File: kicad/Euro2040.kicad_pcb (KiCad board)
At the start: 2 copper layers, 15 x 58.4 mm, 70 parts, among them J1 USB_B_Micro, J3 Conn_02x05_Odd_Even, J5 Conn_01x10_Male, SW1 SW_MEC_5E, U1 RP2040, U2 RT6150B-33GQW, U3 W25Q16JVUXIQ, U4 L7805, U5 TL074, U6 TL074, U7 LM4040DBZ-3, X1 Crystal_GND24

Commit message: save
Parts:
- moved C20 98.9 mm to (-71.2, 21.5)
- moved C22 98.9 mm to (-72.7, 32.4)
- moved R16 98.9 mm to (-52.5, 29.8)
- moved R17 98.9 mm to (-35.6, 37.2)
- moved R18 98.9 mm to (-58.3, 27.8)
- moved R19 98.9 mm to (-52.5, 25.8)
- moved R20 98.9 mm to (-38.5, 37.2)
- moved R21 98.9 mm to (-50.1, 37.2)
- moved R22 98.9 mm to (-41.4, 37.2)
- moved R23 98.9 mm to (-58.3, 25.8)
- moved R24 98.9 mm to (-47.2, 37.2)
- moved R26 98.9 mm to (-52.5, 31.8)
- moved R27 98.9 mm to (-44.3, 37.2)
- moved R29 98.9 mm to (-52.5, 33.8)
- moved R6 98.9 mm to (-52.5, 27.8)
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
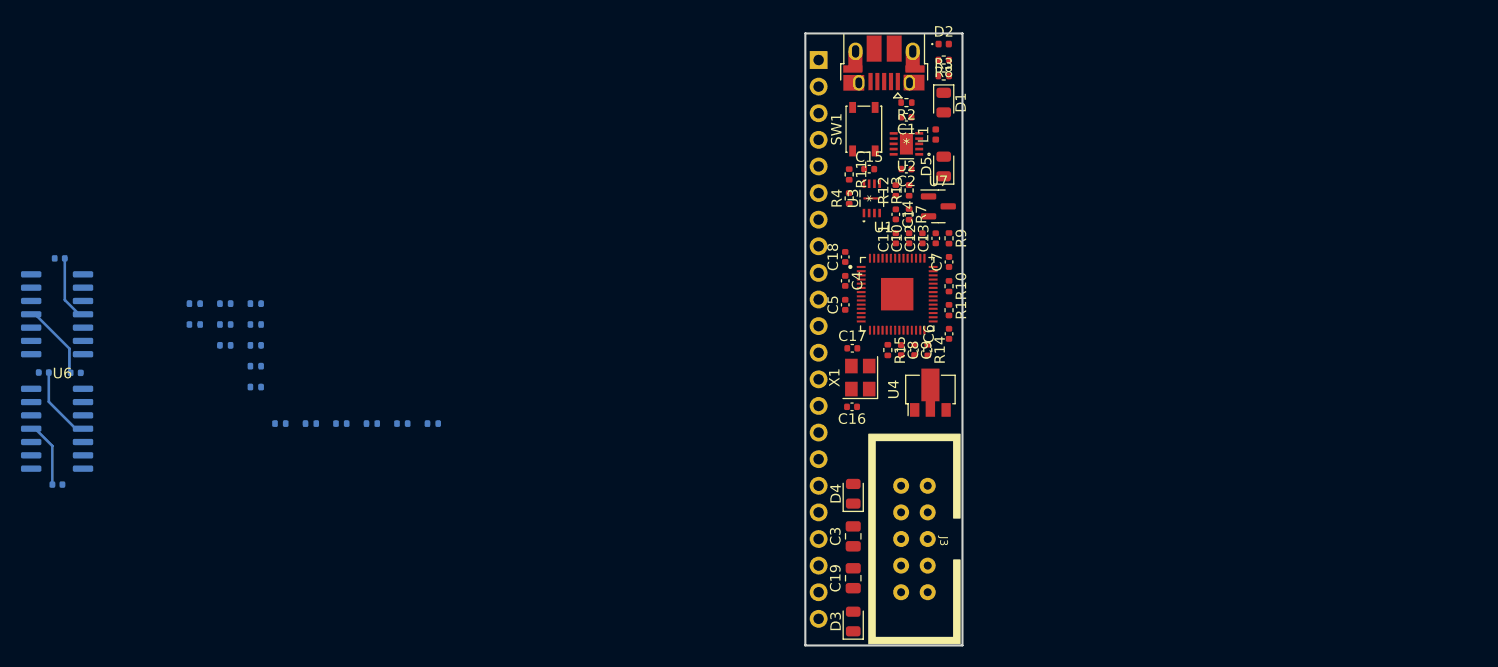
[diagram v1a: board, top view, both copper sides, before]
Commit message: more pins, output RC filter, pcb layout
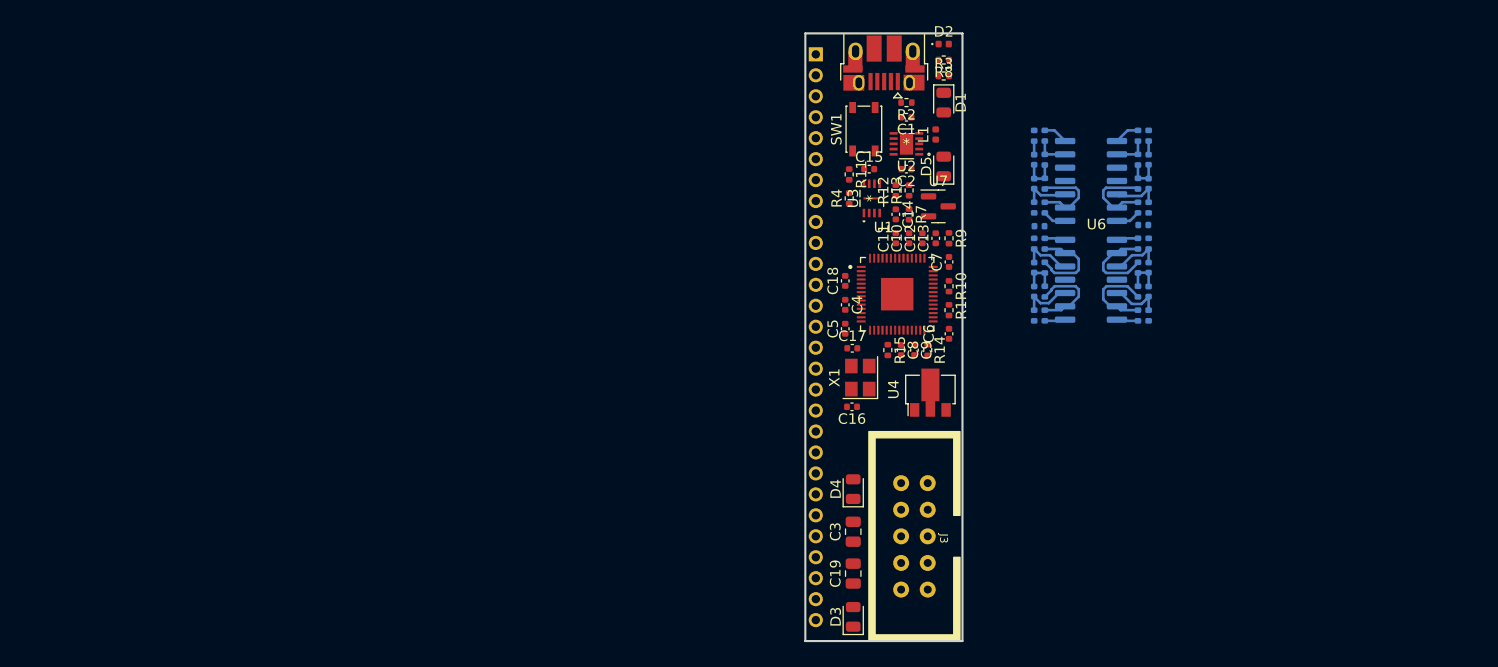
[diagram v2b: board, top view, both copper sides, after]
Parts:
- removed C22, C23: 100n, Capacitor_SMD:C_0402_1005Metric
- added C24: 100n, Capacitor_SMD:C_0402_1005Metric, B.Cu at (32.8, 12.1)
- added C25: 100n, Capacitor_SMD:C_0402_1005Metric, B.Cu at (32.8, 14.3)
- added C26: 100n, Capacitor_SMD:C_0402_1005Metric, B.Cu at (21.8, 14.3)
- added C27: 100n, Capacitor_SMD:C_0402_1005Metric, B.Cu at (21.8, 12.1)
- added C28: 100n, Capacitor_SMD:C_0402_1005Metric, B.Cu at (32.8, 22.4)
- added C29: 100n, Capacitor_SMD:C_0402_1005Metric, B.Cu at (32.8, 24.6)
- added C30: 100n, Capacitor_SMD:C_0402_1005Metric, B.Cu at (21.8, 24.6)
- added C31: 100n, Capacitor_SMD:C_0402_1005Metric, B.Cu at (21.8, 22.4)
- added R30: 1K, Resistor_SMD:R_0402_1005Metric, B.Cu at (32.8, 9.77)
- added R31: 1K, Resistor_SMD:R_0402_1005Metric, B.Cu at (32.8, 16.6)
- added R32: 1K, Resistor_SMD:R_0402_1005Metric, B.Cu at (21.8, 16.6)
- added R33: 1K, Resistor_SMD:R_0402_1005Metric, B.Cu at (21.8, 9.77)
- added R34: 1K, Resistor_SMD:R_0402_1005Metric, B.Cu at (32.8, 20.1)
- added R35: 1K, Resistor_SMD:R_0402_1005Metric, B.Cu at (32.8, 26.9)
- added R36: 1K, Resistor_SMD:R_0402_1005Metric, B.Cu at (21.8, 26.9)
- added R37: 1K, Resistor_SMD:R_0402_1005Metric, B.Cu at (21.8, 20.1)
- J5: footprint Connector_PinHeader_2.54mm:PinHeader_1x22_P2.54mm_Horizontal -> Connector_PinHeader_2.00mm:PinHeader_1x28_P2.00mm_Horizontal
- moved C20 103.5 mm to (32.3, 18.3)
- moved U6 99.7 mm to (27.3, 23.5)
- moved U5 99.5 mm to (27.3, 14.1)
- moved C21 93.1 mm to (22.4, 18.4), turned to 0 degrees
- moved R18 91.8 mm to (31.8, 9.77), turned to 90 degrees
- moved R23 90.0 mm to (31.8, 24.6), turned to 90 degrees
- moved R5 88.2 mm to (31.8, 12.1), turned to -90 degrees
- moved R6 85.3 mm to (31.8, 14.3), turned to 90 degrees
- moved R26 85.0 mm to (31.8, 20.1), turned to 90 degrees
- moved R19 84.7 mm to (31.8, 16.6), turned to -90 degrees
- moved R25 78.4 mm to (22.9, 22.4), turned to -90 degrees
- moved R28 78.3 mm to (22.9, 26.9), turned to -90 degrees
- moved R21 78.0 mm to (22.9, 9.77), turned to 90 degrees
- moved R16 76.9 mm to (22.9, 14.3), turned to 90 degrees
- moved R27 76.7 mm to (31.8, 26.9), turned to -90 degrees
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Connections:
- J5 pad 1: /3V3 -> /GPIO_26_ADC0
- J5 pad 10: /GPIO_3 -> /GPIO_5
- J5 pad 11: /GPIO_4 -> /GPIO_6
- J5 pad 12: /GPIO_5 -> /GPIO_7
- J5 pad 13: /GPIO_6 -> /GPIO_8
- J5 pad 14: /GPIO_7 -> /GPIO_9
- J5 pad 15: /GPIO_8 -> /GPIO_10
- J5 pad 16: /GPIO_9 -> /GPIO_11
- J5 pad 17: /GPIO_10 -> /GPIO_12
- J5 pad 18: /GPIO_11 -> /GPIO_13
- J5 pad 19: /V_7805 -> /GPIO_14
- J5 pad 2: /GPIO_26_ADC0 -> /GPIO_27_ADC0
- J5 pad 20: +12V -> /GPIO_15
- J5 pad 21: -12V -> Earth
- J5 pad 22: Earth -> /USB_D+
- J5 pad 3: /GPIO_27_ADC0 -> /GPIO_28_ADC0
- J5 pad 4: /GPIO_28_ADC0 -> /GPIO_26_ADC0
- J5 pad 5: /GPIO_26_ADC0 -> /GPIO_0
- J5 pad 6: Earth -> /GPIO_1
- J5 pad 7: /GPIO_0 -> /GPIO_2
- J5 pad 8: /GPIO_1 -> /GPIO_3
- J5 pad 9: /GPIO_2 -> /GPIO_4
- U5 pad 10: /GPIO_2X -> Net-(U5-Pad10)
- U5 pad 12: /GPIO_3X -> Net-(U5-Pad12)
- U5 pad 3: /GPIO_0X -> Net-(U5-Pad3)
- U5 pad 5: /GPIO_1X -> Net-(U5-Pad5)
- U6 pad 10: /GPIO_6X -> Net-(U6-Pad10)
- U6 pad 12: /GPIO_7X -> Net-(U6-Pad12)
- U6 pad 3: /GPIO_4X -> Net-(U6-Pad3)
- U6 pad 5: /GPIO_5X -> Net-(U6-Pad5)
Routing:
- net Earth: track 0.00 -> 14.5 mm
- net -12V: track 13.8 -> 0.00 mm
- net +12V: track 13.4 -> 0.00 mm
- net Net-(R23-Pad1): track 0.00 -> 8.54 mm
- net Net-(R25-Pad1): track 0.00 -> 8.53 mm
- net Net-(R22-Pad1): track 0.00 -> 8.42 mm
- net Net-(R24-Pad1): track 0.00 -> 8.29 mm
- net Net-(R19-Pad1): track 0.00 -> 8.07 mm
- net Net-(R16-Pad1): track 0.00 -> 7.93 mm
- net Net-(U6-Pad5): track 0.00 -> 5.05 mm
- net Net-(U6-Pad3): track 0.00 -> 5.00 mm
- net Net-(U6-Pad12): track 0.00 -> 4.94 mm
- net Net-(U6-Pad10): track 0.00 -> 4.93 mm
- net Net-(U5-Pad5): track 0.00 -> 4.67 mm
- net Net-(U5-Pad10): track 0.00 -> 4.54 mm
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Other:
- board size 15 x 58.4 mm -> 15 x 58 mm
- board text added: "3v shunt"
- board text added: "3v3 reg"
- board text added: "5V reg"
- board text added: "RP2040"
- board text added: "bootsel"
- board text added: "crystal"
- board text added: "flash"
